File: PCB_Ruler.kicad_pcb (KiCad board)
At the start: 2 copper layers, 100.5 x 27 mm, 81 parts, among them Q1 SOT23-3, Q10 SOT89, Q11 SOT886, Q12 SOT963, Q13 SSOP-16, Q14 SSOP-8, Q15 SOT1113, Q16 SOT665, Q2 SOT23-5, Q3 SOT323, Q4 SOT353, Q5 SOT553, Q6 DPAK, Q7 DP2AK, Q8 LFPAK, Q9 SOT223, U1 1.00, U10 5mm, U11 6mm, U12 7mm, U13 8mm, U14 9mm, U15 3_10in, U16 0_16in, U17 1_16in, U18 2_16in, U19 3_16in, U2 1.27, U20 0_10in, U21 1_10in, U22 2_10in, U3 2.00, U4 2.54, U5 0mm, U6 1mm, U7 2mm, U8 3mm, U9 4mm

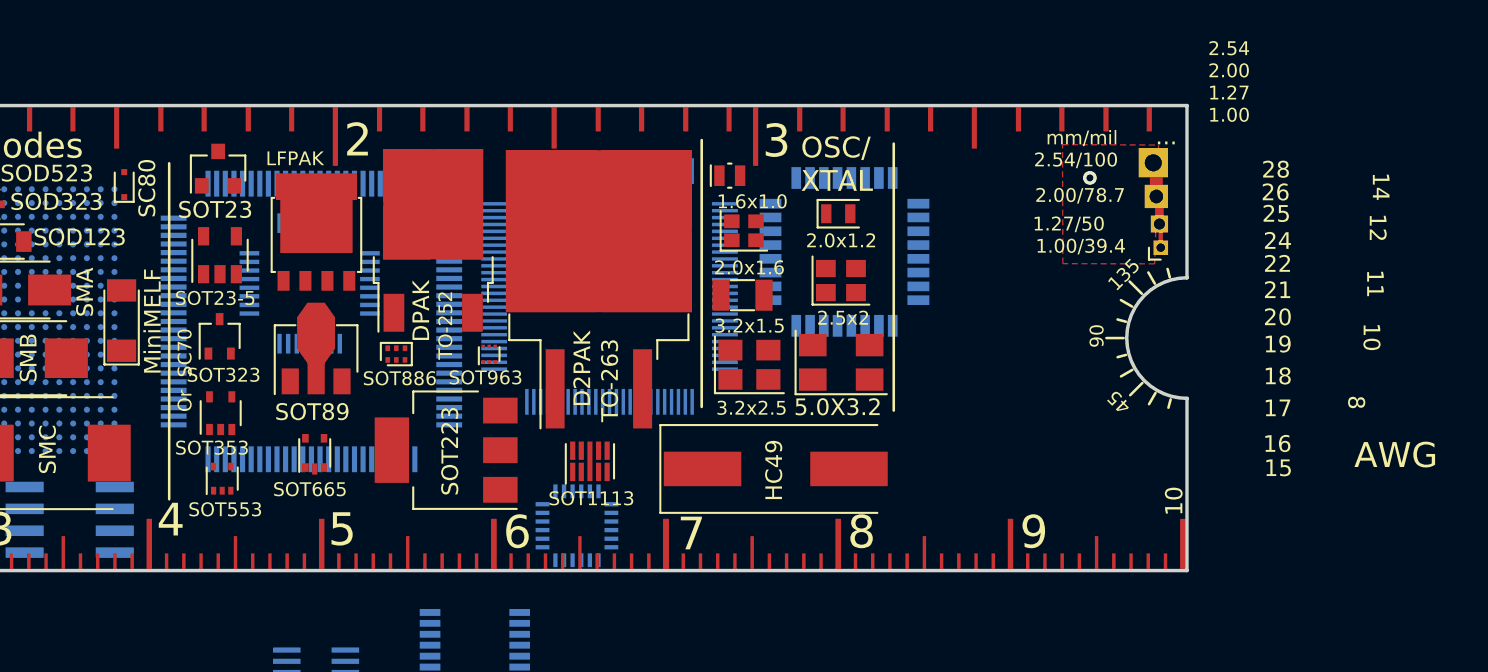
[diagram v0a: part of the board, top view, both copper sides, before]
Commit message: Finished top side, still have room for more parts...
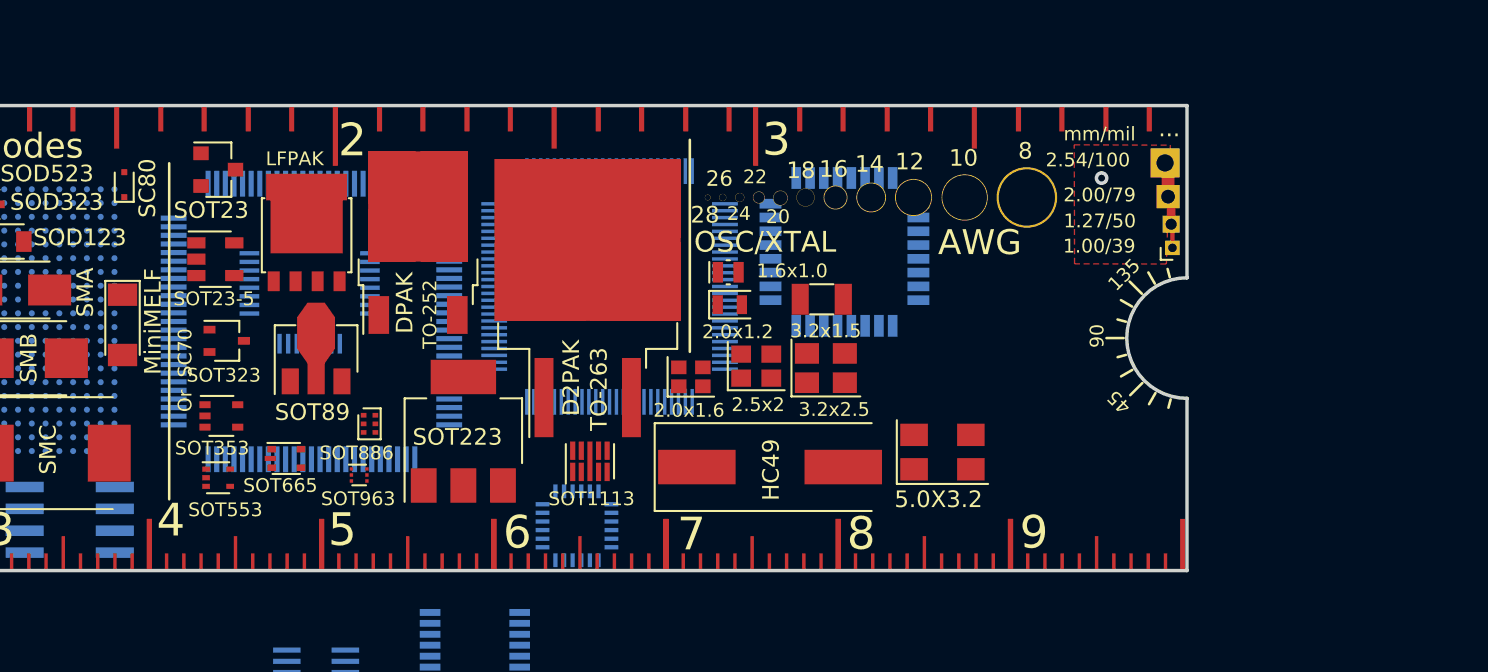
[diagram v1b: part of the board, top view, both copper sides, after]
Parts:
- added H1: 08AWG, PCB_Ruler:Mounting_Hole_8AWG, F.Cu at (161.2, 96.0)
- added H10: 26AWG, PCB_Ruler:Mounting_Hole_26AWG, F.Cu at (143.5, 96.0)
- added H11: 28AWG, PCB_Ruler:Mounting_Hole_28AWG, F.Cu at (142.7, 96.0)
- added H2: 10AWG, PCB_Ruler:Mounting_Hole_10AWG, F.Cu at (157.6, 96.0)
- added H3: 12AWG, PCB_Ruler:Mounting_Hole_12AWG, F.Cu at (154.6, 96.0)
- added H4: 14AWG, PCB_Ruler:Mounting_Hole_14AWG, F.Cu at (152.2, 96.0)
- added H5: 16AWG, PCB_Ruler:Mounting_Hole_16AWG, F.Cu at (150.1, 96.1)
- added H6: 18AWG, PCB_Ruler:Mounting_Hole_18AWG, F.Cu at (148.3, 96.0)
- added H7: 20AWG, PCB_Ruler:Mounting_Hole_20AWG, F.Cu at (144.6, 98.4)
- added H8: 22AWG, PCB_Ruler:Mounting_Hole_22AWG, F.Cu at (145.6, 96.0)
- added H9: 24AWG, PCB_Ruler:Mounting_Hole_24AWG, F.Cu at (144.5, 96.0)
- U10, U11, U12, U13, U14, U5, U6, U7, U8, U9: footprint Adafruit PCB Reference Ruler:EDGE-MILLIMETERS -> PCB_Ruler:EDGE-MILLIMETERS
- U15, U20, U21, U22: footprint Adafruit PCB Reference Ruler:EDGE-INCHES-TENTH -> PCB_Ruler:EDGE-INCHES-TENTH
- U16, U17, U18, U19: footprint Adafruit PCB Reference Ruler:EDGE-INCHES-SIXTEENTH -> PCB_Ruler:EDGE-INCHES-SIXTEENTH
- moved Q12 10.3 mm to (122.4, 114.5), turned to 0 degrees
- moved XT4 9.02 mm to (141.7, 108.8)
- moved XT3 8.22 mm to (143.9, 104.6)
- moved XT6 7.86 mm to (156.3, 113.1)
- moved XT7 6.99 mm to (145.5, 108.1)
- moved XT2 5.61 mm to (143.9, 102.7)
- moved XT8 4.61 mm to (149.3, 104.2)
- moved XT5 4.44 mm to (149.5, 108.2)
- moved Q11 4.34 mm to (123.0, 111.5), turned to 0 degrees
- moved Q16 1.68 mm to (118.2, 113.5), turned to 0 degrees
- moved Q9 1.49 mm to (128.5, 111.9), turned to 90 degrees
- moved Q6 0.89 mm to (125.8, 101.0)
- moved Q7 0.83 mm to (135.7, 104.2)
- moved U1 0.68 mm to (169.7, 101.3)
- moved U2 0.68 mm to (169.6, 99.9)
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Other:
- board text added: "1.00/39"
- board text added: "2.00/79"
- board text added: "OSC/XTAL"
- board text removed: "1.00/39.4"
- board text removed: "2.00/78.7"
- board text removed: "2.54 2.00 1.27 1.00"
- board text removed: "OSC/ XTAL"

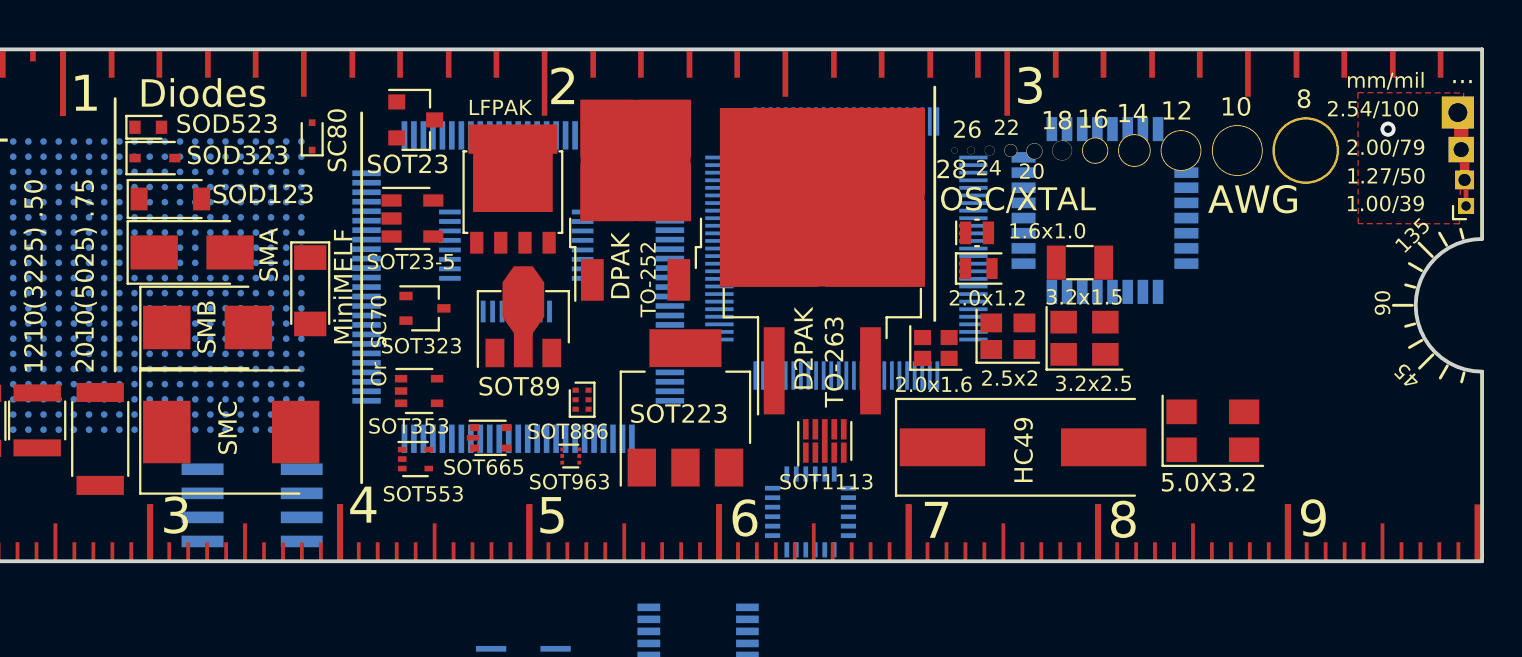
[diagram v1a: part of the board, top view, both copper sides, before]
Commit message: Put text/transistor outlines on top layer
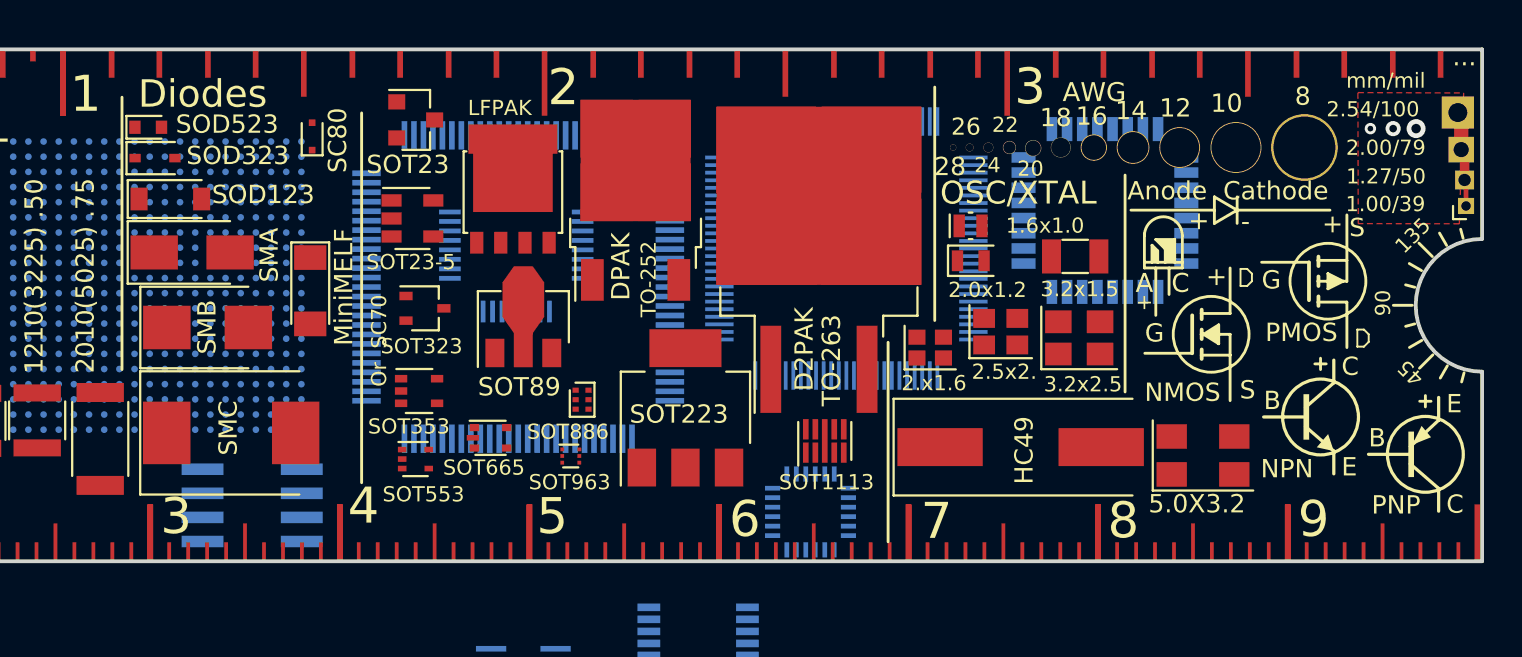
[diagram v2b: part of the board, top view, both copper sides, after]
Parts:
- E$50: footprint Adafruit PCB Reference Ruler:NMOS-SYMB -> PCB_Ruler:NMOS-SYMB; moved to F.Cu
- E$51: footprint Adafruit PCB Reference Ruler:PMOS-SYMB -> PCB_Ruler:PMOS-SYMB; moved to F.Cu
- E$52: moved to F.Cu
- E$53: footprint Adafruit PCB Reference Ruler:LED-GUIDE -> PCB_Ruler:LED-GUIDE; moved to F.Cu
- E$54: footprint Adafruit PCB Reference Ruler:NPN-SYMB -> PCB_Ruler:NPN-SYMB; moved to F.Cu
- E$59: footprint Adafruit PCB Reference Ruler:PNP-SYMB -> PCB_Ruler:PNP-SYMB; moved to F.Cu
- moved E$52 37.2 mm to (157.0, 101.0), turned to 0 degrees
- moved E$53 26.0 mm to (154.1, 105.1), turned to 0 degrees
- moved E$59 23.2 mm to (167.5, 114.4), turned to 0 degrees
- moved E$54 11.8 mm to (162.0, 112.4), turned to 0 degrees
- moved E$51 9.52 mm to (162.4, 105.2), turned to 0 degrees
- moved E$50 3.16 mm to (156.2, 108.0), turned to 0 degrees
- moved XT6 1.40 mm to (155.8, 114.4)
- moved XT3 0.59 mm to (143.5, 104.2)
- moved XT2 0.50 mm to (143.5, 102.3)
- moved XT7 0.45 mm to (145.1, 107.9)
- moved XT8 0.41 mm to (149.0, 103.9)
- moved XT4 0.30 mm to (141.4, 108.7)
- moved XT5 0.28 mm to (149.2, 108.2)
- moved Q7 0.20 mm to (135.5, 104.1)
- moved H7 0.17 mm to (144.5, 98.2)
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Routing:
- net /Via: vias 1 -> 3
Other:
- board text added: "2.5x2."
- board text added: "2.x1.6"
- board text removed: "2.0x1.6"
- board text removed: "2.5x2"

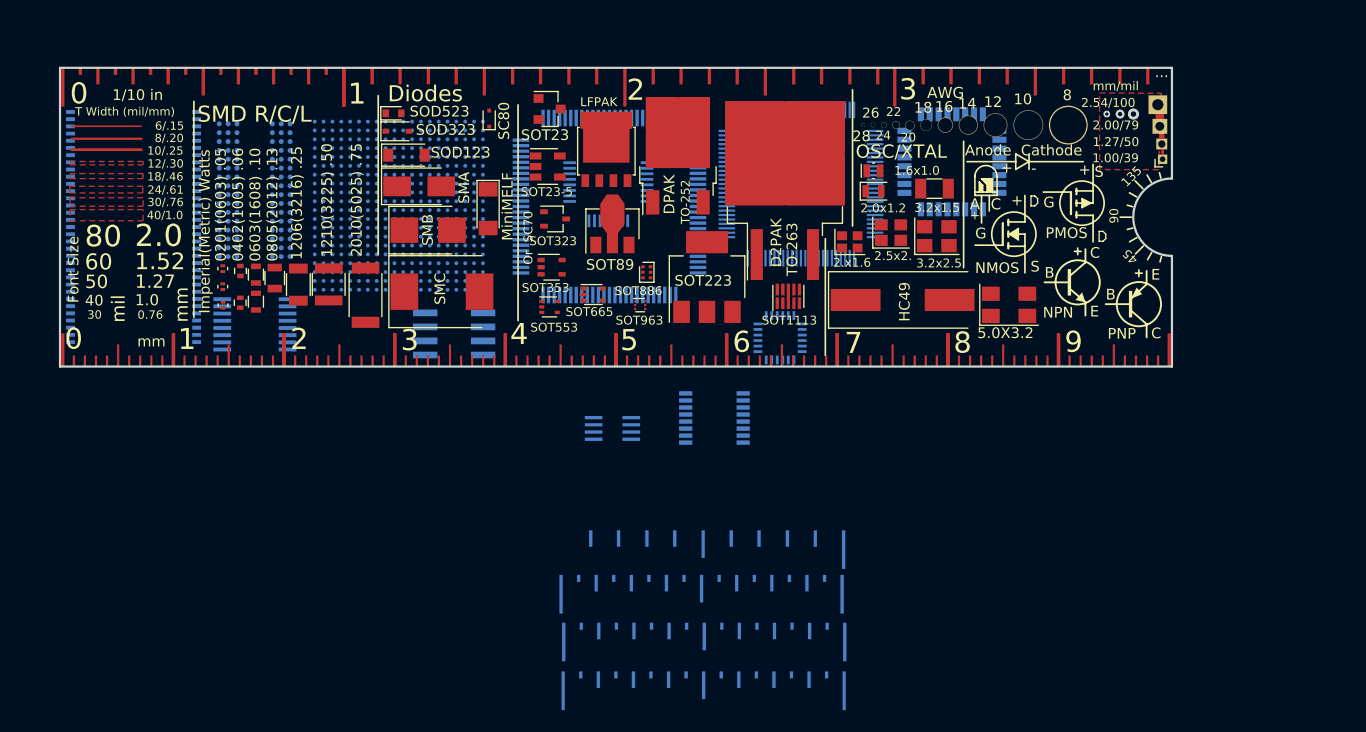
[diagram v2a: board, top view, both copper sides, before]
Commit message: Inches on both sides
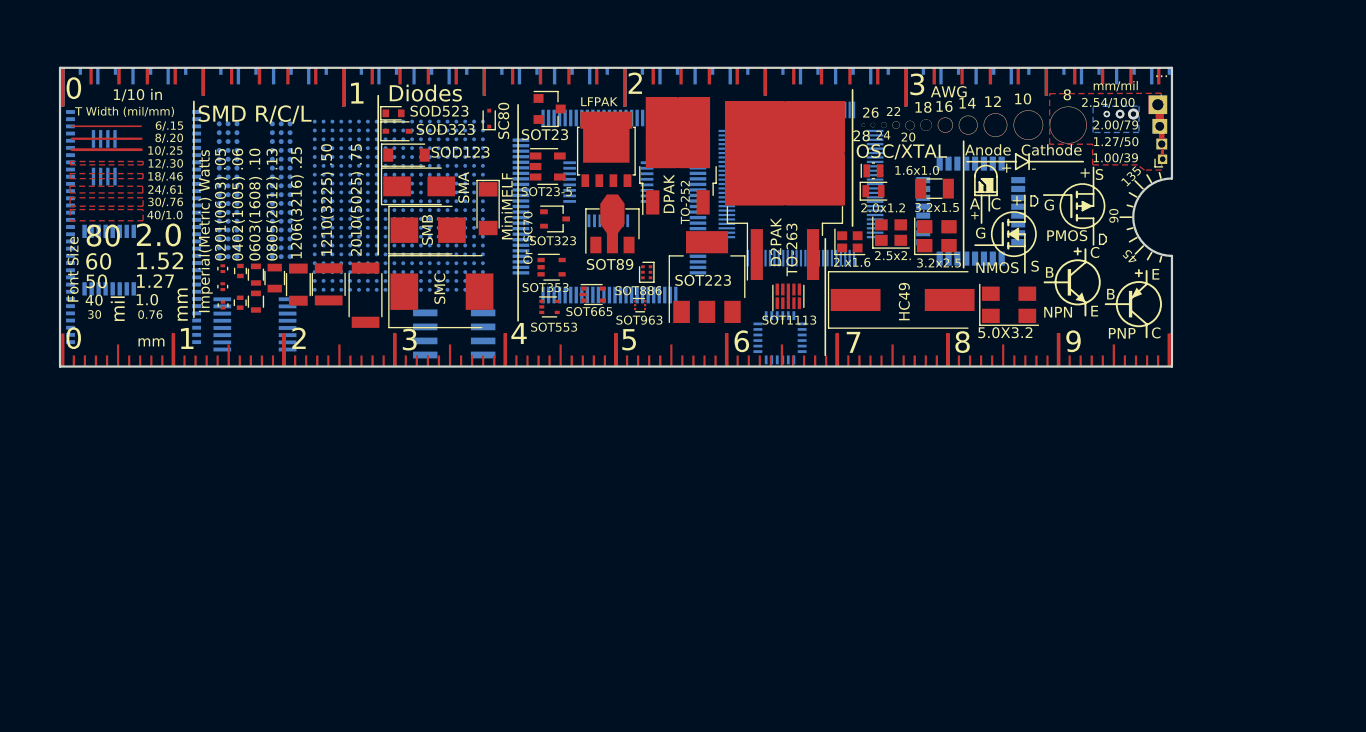
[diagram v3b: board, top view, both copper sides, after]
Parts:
- H1: footprint PCB_Ruler:Mounting_Hole_8AWG -> PCB_Ruler:Mounting_Hole_08AWG
- U15: moved to F.Cu
- U19: moved to B.Cu
- moved U19 101.6 mm to (171.8, 93.0), turned to 180 degrees
- moved U16 64.3 mm to (95.7, 93.0)
- moved Q13 56.5 mm to (74.4, 110.4), turned to 270 degrees
- moved U18 54.8 mm to (146.4, 93.0)
- moved U17 53.9 mm to (121.0, 93.0)
- moved Q14 52.0 mm to (74.0, 101.1), turned to 270 degrees
- moved U15 42.2 mm to (146.4, 93.0), turned to 0 degrees
- moved U20 25.4 mm to (70.2, 93.0)
- moved U21 25.4 mm to (95.7, 93.0)
- moved U22 24.4 mm to (121.0, 93.0)
- moved E$69 4.76 mm to (152.3, 106.0)
- moved E$51 0.27 mm to (162.4, 105.5)
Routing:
- added copper zone on B.Cu, net /Via
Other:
- board text added: "1/16 in"
- board text removed: "11"
- board text removed: "15"
- board text removed: "17"
- board text removed: "19"
- board text removed: "21"
- board text removed: "25"
